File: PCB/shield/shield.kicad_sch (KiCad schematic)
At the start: 19 parts, among them J1 QTR-8A, J10 ESP32_left_m, J11 ESP32_right_m, J13 Conn_01x06, J14 Domino, J15 Domino, J2 QMC5883L, J3 Servo, J4 Domino, J8 ESP32_left_f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

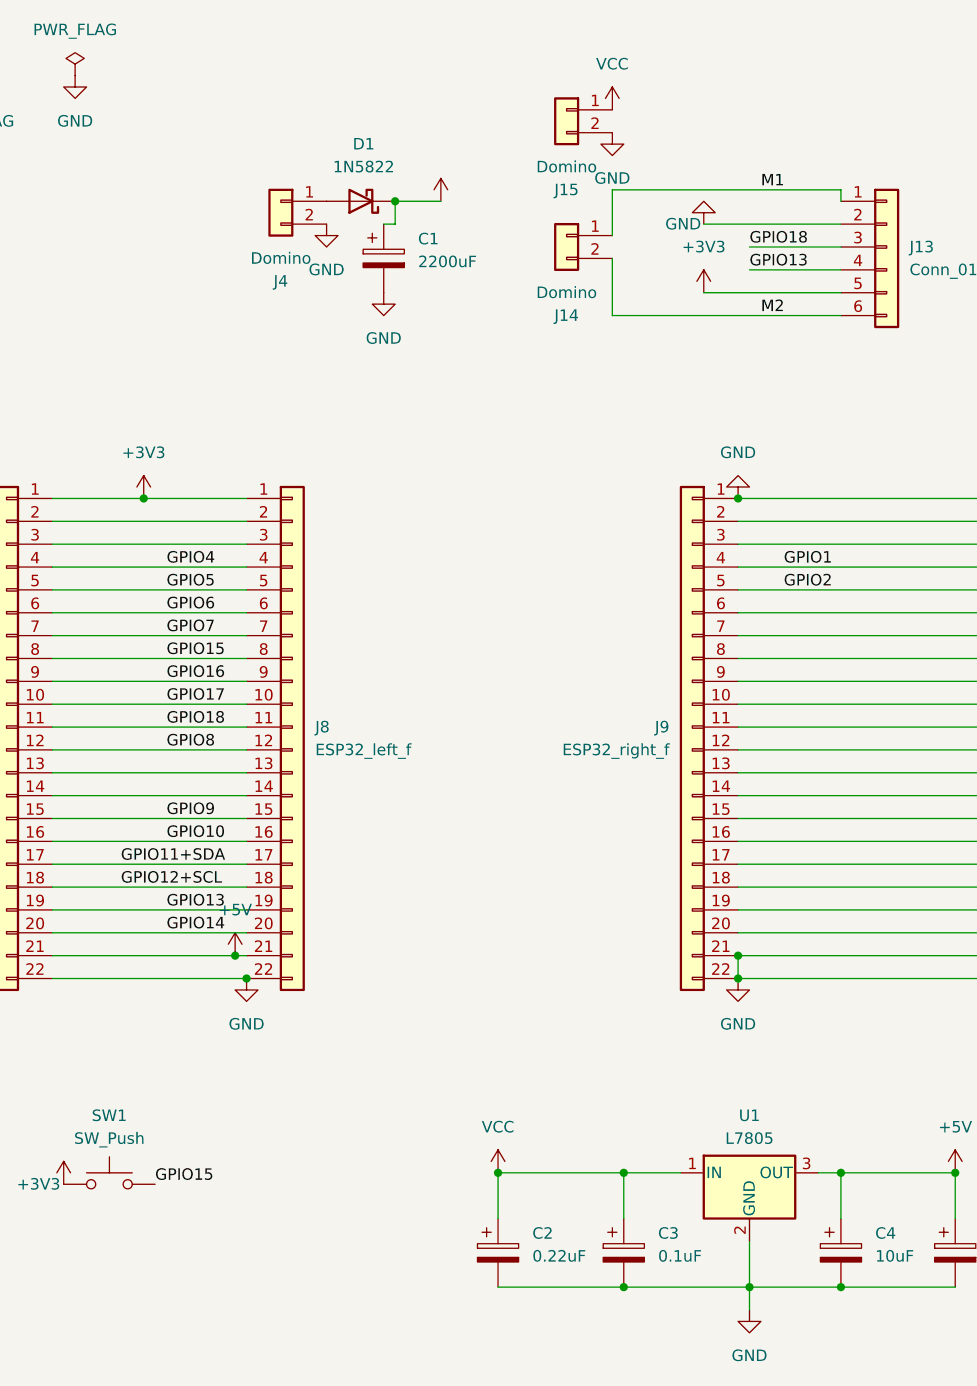
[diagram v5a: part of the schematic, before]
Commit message: feat: change THT to SMD
Changed LM7805 to AMS1117
Changed THT capacitor to SMD capacitor
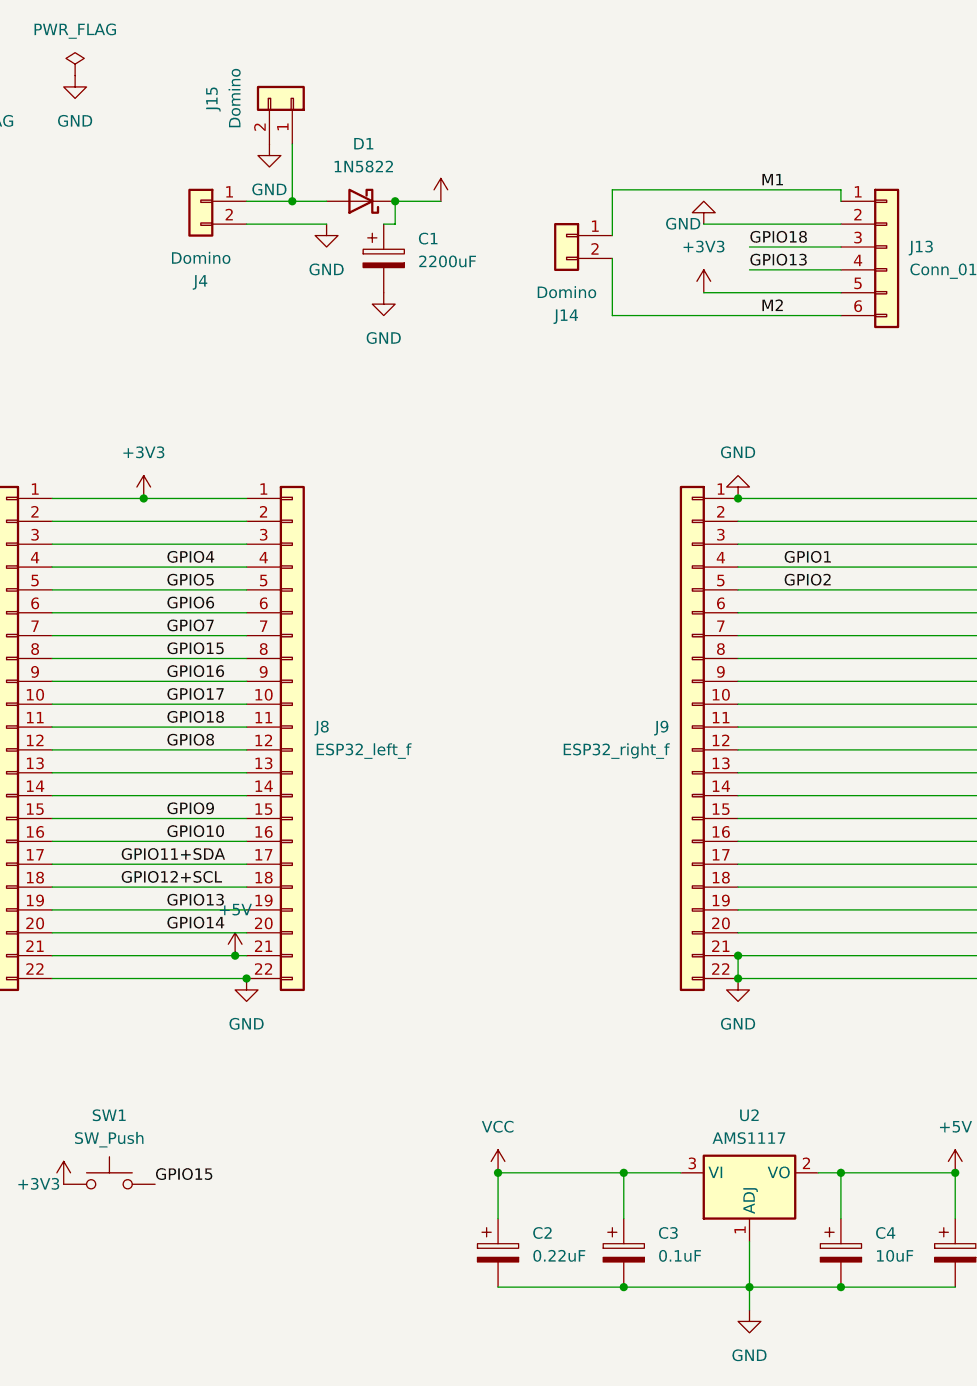
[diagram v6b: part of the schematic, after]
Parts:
- removed U1: L7805, Package_TO_SOT_THT:TO-220-3_Vertical, symbol Regulator_Linear:L7805
- added U2: AMS1117, Package_TO_SOT_SMD:SOT-223-3_TabPin2, symbol Regulator_Linear:AMS1117
- C2, C4: footprint Capacitor_THT:CP_Radial_D5.0mm_P2.00mm -> Capacitor_SMD:C_0805_2012Metric_Pad1.18x1.45mm_HandSolder
- C3, C5: footprint Capacitor_THT:CP_Radial_Tantal_D4.5mm_P2.50mm -> Capacitor_SMD:C_0805_2012Metric_Pad1.18x1.45mm_HandSolder
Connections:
- net +5V: now also U2.2 (VO)
- net GND: now also U2.1 (ADJ)
- net VCC: now also U2.3 (VI); no longer J15.1 (Pin_1)
- net at D1.2 (A), J4.1 (Pin_1): now also J15.1 (Pin_1)
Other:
- moved on the sheet: J15, J4
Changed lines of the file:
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@@
 	)
 	(junction
+		(at 87.63 39.37)
+		(diameter 0)
+		(color 0 0 0 0)
+	)
+	(junction
 		(at 138.43 160.02)
 		(diameter 0)
@@
 	(wire
 		(pts
+			(xy 82.55 41.91) (xy 91.44 41.91)
+		)
+		(stroke
+			(width 0)
+			(type default)
+		)
+	)
+	(wire
+		(pts
 			(xy 60.96 123.19) (xy 81.28 123.19)
 		)
@@
 	(wire
 		(pts
+			(xy 82.55 39.37) (xy 87.63 39.37)
+		)
+		(stroke
+			(width 0)
+			(type default)
+		)
+	)
+	(wire
+		(pts
 			(xy 138.43 46.99) (xy 148.59 46.99)
 		)
@@
 	(wire
 		(pts
+			(xy 87.63 39.37) (xy 91.44 39.37)
+		)
+		(stroke
+			(width 0)
+			(type default)
+		)
+	)
+	(wire
+		(pts
 			(xy 166.37 80.01) (xy 137.16 80.01)
 		)
@@
 	(wire
 		(pts
+			(xy 87.63 33.02) (xy 87.63 39.37)
+		)
+		(stroke
+			(width 0)
+			(type default)
+		)
+	)
+	(wire
+		(pts
 			(xy 60.96 82.55) (xy 82.55 82.55)
 		)
@@
 			)
 		)
-		(property "Footprint" "Capacitor_THT:CP_Radial_Tantal_D4.5mm_P2.50mm"
+		(property "Footprint" "Capacitor_SMD:C_0805_2012Metric_Pad1.18x1.45mm_HandSolder"
 			(at 162.2552 160.02 0)
 			(effects
@@
 	)
 	(symbol
-		(lib_id "power:VCC")
-		(at 123.19 29.21 0)
-		(unit 1)
-		(exclude_from_sim no)
-		(in_bom yes)
-		(on_board yes)
-		(dnp no)
-		(fields_autoplaced yes)
-		(property "Reference" "#PWR022"
-			(at 123.19 33.02 0)
-			(effects
-				(font
-					(size 1.27 1.27)
-				)
-				(hide yes)
-			)
-		)
-		(property "Value" "VCC"
-			(at 123.19 24.13 0)
-			(effects
-				(font
-					(size 1.27 1.27)
-				)
-			)
-		)
-		(property "Footprint" ""
-			(at 123.19 29.21 0)
-			(effects
-				(font
-					(size 1.27 1.27)
-				)
-				(hide yes)
-			)
-		)
-		(property "Datasheet" ""
-			(at 123.19 29.21 0)
-			(effects
-				(font
-					(size 1.27 1.27)
-				)
-				(hide yes)
-			)
-		)
-		(property "Description" "Power symbol creates a global label with name \"VCC\""
-			(at 123.19 29.21 0)
-			(effects
-				(font
-					(size 1.27 1.27)
-				)
-				(hide yes)
-			)
-		)
-		(pin "1"
-		)
-		(instances
-			(project ""
-				(path "/9a41b561-8e6b-4187-bd8f-1a6b5b887c54"
-					(reference "#PWR022")
-					(unit 1)
-				)
-			)
-		)
-	)
-	(symbol
 		(lib_id "Connector_Generic:Conn_01x03")
 		(at 228.6 120.65 0)
@@
 	(symbol
 		(lib_id "Connector_Generic:Conn_01x02")
-		(at 118.11 29.21 0)
-		(mirror y)
+		(at 87.63 27.94 270)
+		(mirror x)
 		(unit 1)
 		(exclude_from_sim no)
@@
 		(dnp no)
 		(property "Reference" "J15"
-			(at 118.11 38.1 0)
+			(at 78.74 27.94 0)
 			(effects
 				(font
@@
 		)
 		(property "Value" "Domino"
-			(at 118.11 35.56 0)
+			(at 81.28 27.94 0)
 			(effects
 				(font
@@
 		)
 		(property "Footprint" "TerminalBlock_Phoenix:TerminalBlock_Phoenix_MKDS-1,5-2_1x02_P5.00mm_Horizontal"
-			(at 118.11 29.21 0)
+			(at 87.63 27.94 0)
 			(effects
 				(font
@@
 		)
 		(property "Datasheet" "~"
-			(at 118.11 29.21 0)
+			(at 87.63 27.94 0)
 			(effects
 				(font
@@
 		)
 		(property "Description" "Generic connector, single row, 01x02, script generated (kicad-library-utils/schlib/autogen/connector/)"
-			(at 118.11 29.21 0)
+			(at 87.63 27.94 0)
 			(effects
 				(font
@@
 	(symbol
 		(lib_id "Connector_Generic:Conn_01x02")
-		(at 86.36 39.37 0)
+		(at 77.47 39.37 0)
 		(mirror y)
 		(unit 1)
@@
 		(dnp no)
 		(property "Reference" "J4"
-			(at 86.36 48.26 0)
+			(at 77.47 48.26 0)
 			(effects
 				(font
@@
 		)
 		(property "Value" "Domino"
-			(at 86.36 45.72 0)
+			(at 77.47 45.72 0)
 			(effects
 				(font
@@
 		)
 		(property "Footprint" "TerminalBlock_Phoenix:TerminalBlock_Phoenix_MKDS-1,5-2_1x02_P5.00mm_Horizontal"
-			(at 86.36 39.37 0)
+			(at 77.47 39.37 0)
 			(effects
 				(font
@@
 		)
 		(property "Datasheet" "~"
-			(at 86.36 39.37 0)
+			(at 77.47 39.37 0)
 			(effects
 				(font
@@
 		)
 		(property "Description" "Generic connector, single row, 01x02, script generated (kicad-library-utils/schlib/autogen/connector/)"
-			(at 86.36 39.37 0)
+			(at 77.47 39.37 0)
 			(effects
 				(font
@@
 			)
 		)
-		(property "Footprint" "Capacitor_THT:CP_Radial_Tantal_D4.5mm_P2.50mm"
+		(property "Footprint" "Capacitor_SMD:C_0805_2012Metric_Pad1.18x1.45mm_HandSolder"
 			(at 125.4252 160.02 0)
 			(effects
@@
 			)
 		)
-		(property "Footprint" "Capacitor_THT:CP_Radial_D5.0mm_P2.00mm"
+		(property "Footprint" "Capacitor_SMD:C_0805_2012Metric_Pad1.18x1.45mm_HandSolder"
 			(at 149.5552 160.02 0)
 			(effects
@@
 	)
 	(symbol
-		(lib_id "Regulator_Linear:L7805")
-		(at 138.43 147.32 0)
-		(unit 1)
-		(exclude_from_sim no)
-		(in_bom yes)
-		(on_board yes)
-		(dnp no)
-		(fields_autoplaced yes)
-		(property "Reference" "U1"
-			(at 138.43 140.97 0)
-			(effects
-				(font
-					(size 1.27 1.27)
-				)
-			)
-		)
-		(property "Value" "L7805"
-			(at 138.43 143.51 0)
-			(effects
-				(font
-					(size 1.27 1.27)
-				)
-			)
-		)
-		(property "Footprint" "Package_TO_SOT_THT:TO-220-3_Vertical"
-			(at 139.065 151.13 0)
-			(effects
-				(font
-					(size 1.27 1.27)
-					(italic yes)
-				)
-				(justify left)
-				(hide yes)
-			)
-		)
-		(property "Datasheet" "http://www.st.com/content/ccc/resource/technical/document/datasheet/41/4f/b3/b0/12/d4/47/88/CD00000444.pdf/files/CD00000444.pdf/jcr:content/translations/en.CD00000444.pdf"
-			(at 138.43 148.59 0)
-			(effects
-				(font
-					(size 1.27 1.27)
-				)
-				(hide yes)
-			)
-		)
-		(property "Description" "Positive 1.5A 35V Linear Regulator, Fixed Output 5V, TO-220/TO-263/TO-252"
-			(at 138.43 147.32 0)
-			(effects
-				(font
-					(size 1.27 1.27)
-				)
-				(hide yes)
-			)
-		)
-		(pin "2"
-		)
-		(pin "1"
-		)
-		(pin "3"
-		)
-		(instances
-			(project ""
-				(path "/9a41b561-8e6b-4187-bd8f-1a6b5b887c54"
-					(reference "U1")
-					(unit 1)
-				)
-			)
-		)
-	)
-	(symbol
 		(lib_id "Connector_Generic:Conn_01x05")
 		(at 207.01 86.36 0)
@@
 	(symbol
 		(lib_id "power:GND")
-		(at 123.19 31.75 0)
+		(at 85.09 33.02 0)
 		(unit 1)
 		(exclude_from_sim no)
@@
 		(on_board yes)
 		(dnp no)
-		(fields_autoplaced yes)
 		(property "Reference" "#PWR023"
-			(at 123.19 38.1 0)
+			(at 85.09 39.37 0)
 			(effects
 				(font
@@
 		)
 		(property "Value" "GND"
-			(at 123.19 36.83 0)
+			(at 85.09 38.1 0)
 			(effects
 				(font
@@
 		)
 		(property "Footprint" ""
-			(at 123.19 31.75 0)
+			(at 85.09 33.02 0)
 			(effects
 				(font
@@
 		)
 		(property "Datasheet" ""
-			(at 123.19 31.75 0)
+			(at 85.09 33.02 0)
 			(effects
 				(font
@@
 		)
 		(property "Description" "Power symbol creates a global label with name \"GND\" , ground"
-			(at 123.19 31.75 0)
+			(at 85.09 33.02 0)
 			(effects
 				(font
@@
 			)
 		)
-		(property "Footprint" "Capacitor_THT:CP_Radial_D5.0mm_P2.00mm"
+		(property "Footprint" "Capacitor_SMD:C_0805_2012Metric_Pad1.18x1.45mm_HandSolder"
 			(at 111.4552 160.02 0)
 			(effects
@@
 					(unit 1)
 				)
+			)
+		)
+	)
+	(symbol
+		(lib_id "Regulator_Linear:AMS1117")
+		(at 138.43 147.32 0)
+		(unit 1)
+		(exclude_from_sim no)
+		(in_bom yes)
+		(on_board yes)
+		(dnp no)
+		(fields_autoplaced yes)
+		(property "Reference" "U2"
+			(at 138.43 140.97 0)
+			(effects
+				(font
+					(size 1.27 1.27)
+				)
+			)
+		)
+		(property "Value" "AMS1117"
+			(at 138.43 143.51 0)
+			(effects
+				(font
+					(size 1.27 1.27)
+				)
+			)
+		)
+		(property "Footprint" "Package_TO_SOT_SMD:SOT-223-3_TabPin2"
+			(at 138.43 142.24 0)
+			(effects
+				(font
+					(size 1.27 1.27)
+				)
+				(hide yes)
+			)
+		)
+		(property "Datasheet" "http://www.advanced-monolithic.com/pdf/ds1117.pdf"
+			(at 140.97 153.67 0)
+			(effects
+				(font
+					(size 1.27 1.27)
+				)
+				(hide yes)
+			)
+		)
+		(property "Description" "1A Low Dropout regulator, positive, adjustable output, SOT-223"
+			(at 138.43 147.32 0)
+			(effects
+				(font
+					(size 1.27 1.27)
+				)
+				(hide yes)
+			)
+		)
+		(pin "3"
+		)
+		(pin "2"
+		)
+		(pin "1"
+		)
+		(instances
+			(project ""
+				(path "/9a41b561-8e6b-4187-bd8f-1a6b5b887c54"
+					(reference "U2")
+					(unit 1)
+				)

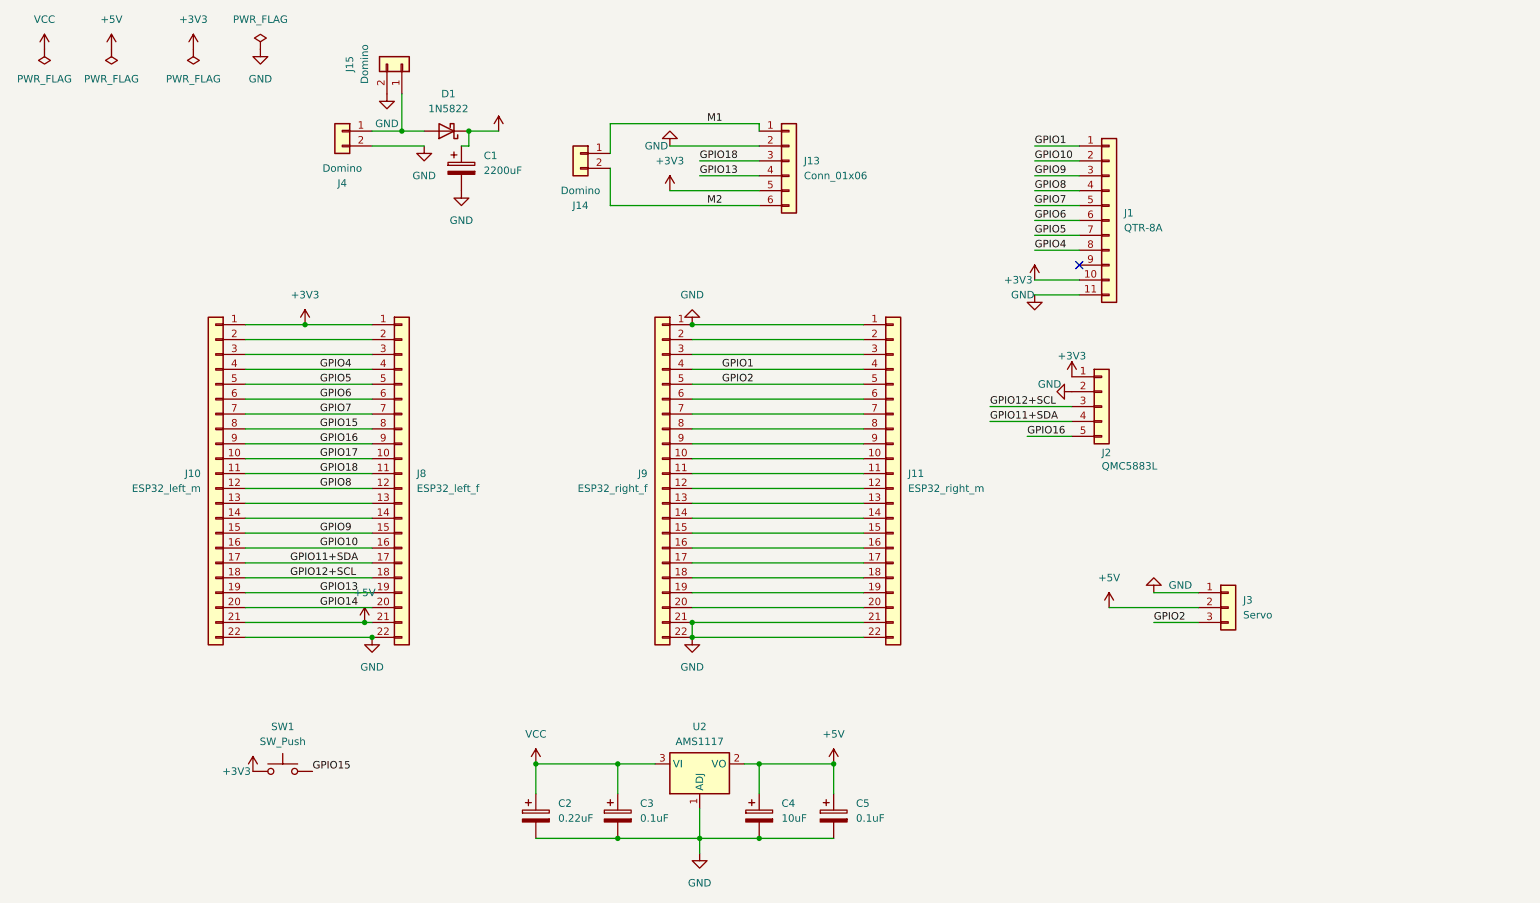
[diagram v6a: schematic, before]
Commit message: feat: added socket for joystick module
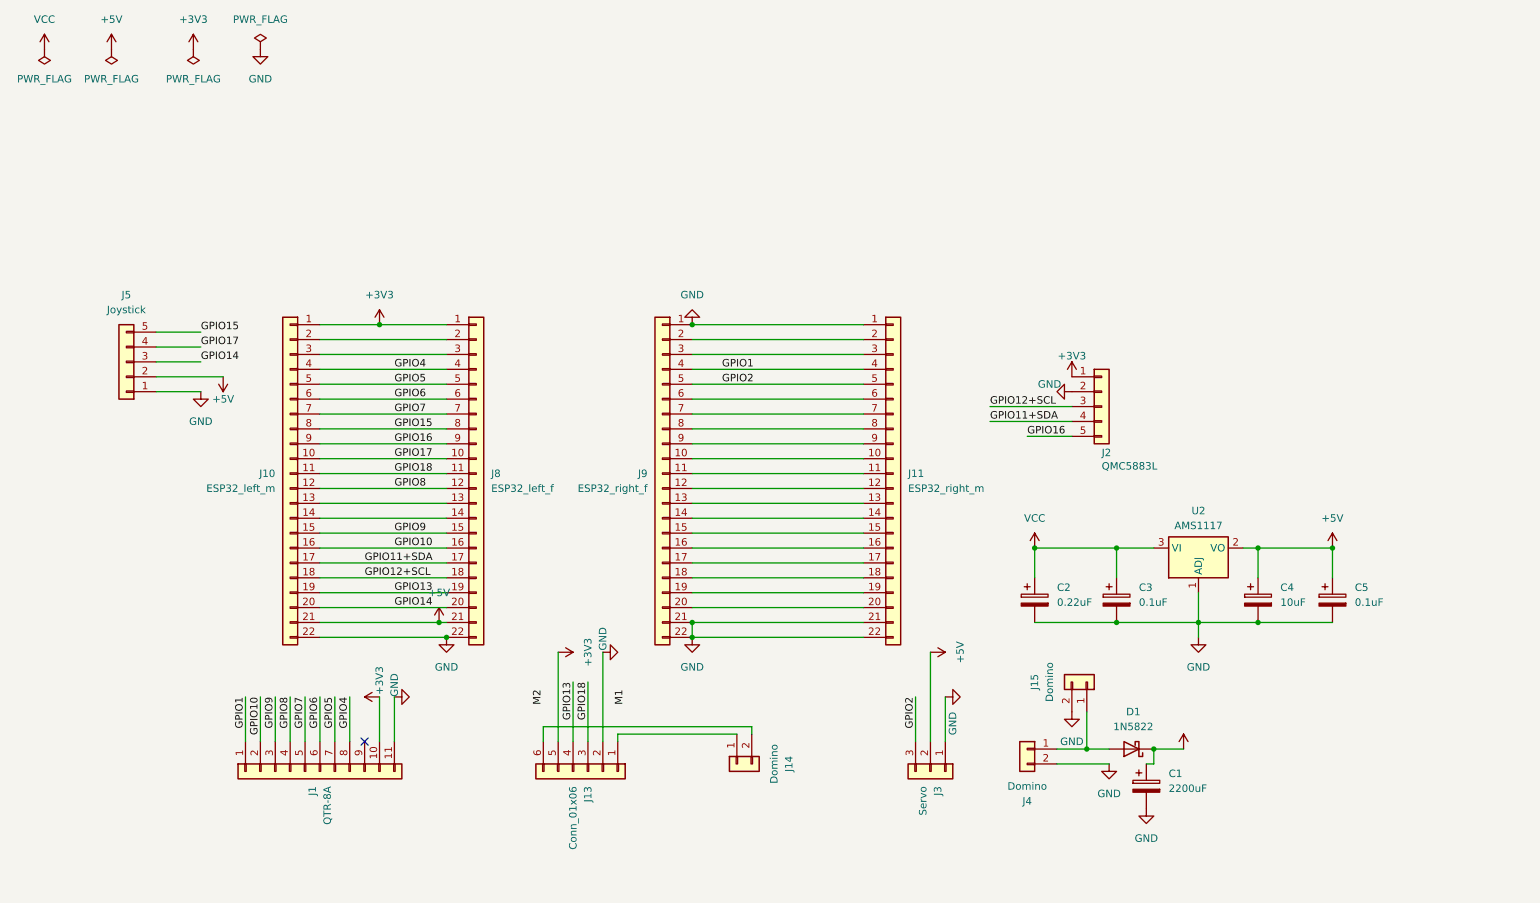
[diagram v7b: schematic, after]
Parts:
- removed SW1: SW_Push, Button_Switch_THT:SW_PUSH_6mm_H5mm, symbol Switch:SW_Push
- added J5: Joystick, Connector_PinSocket_2.54mm:PinSocket_1x05_P2.54mm_Vertical, symbol Connector_Generic:Conn_01x05
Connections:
- net +5V: now also J5.2 (Pin_2)
- net GND: now also J5.1 (Pin_1)
- net GPIO14: now also J5.3 (Pin_3)
- net GPIO15: now also J5.5 (Pin_5)
- net GPIO17: now also J5.4 (Pin_4)
- net M1: no longer J13.1 (Pin_1), J14.1 (Pin_1)
- net M2: no longer J13.6 (Pin_6), J14.2 (Pin_2)
- new net: J13.1 (Pin_1), J14.1 (Pin_1)
- new net: J13.6 (Pin_6), J14.2 (Pin_2)
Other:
- moved on the sheet: C1, C2, C3, C4, C5, D1, J1, J10, J13, J14, J15, J3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

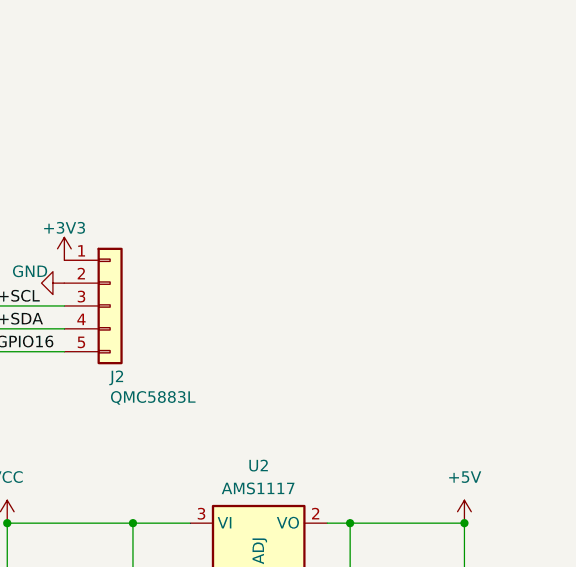
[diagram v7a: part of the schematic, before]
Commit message: feat: add lcd oled screen socket
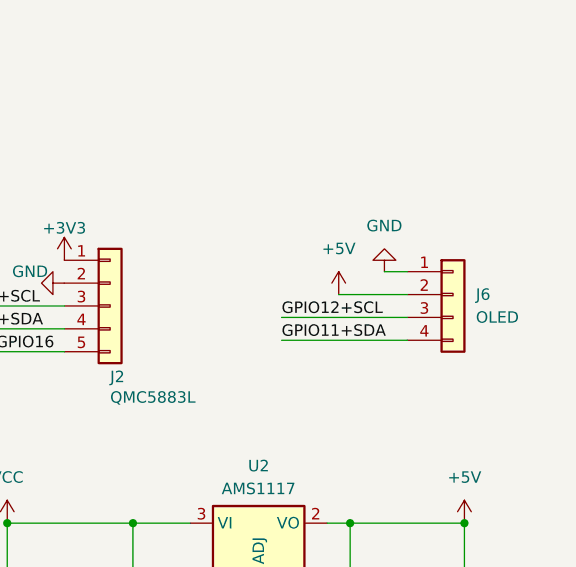
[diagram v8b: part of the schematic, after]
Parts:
- added J6: OLED, Connector_PinSocket_2.54mm:PinSocket_1x04_P2.54mm_Vertical, symbol Connector_Generic:Conn_01x04
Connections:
- net +5V: now also J6.2 (Pin_2)
- net GND: now also J6.1 (Pin_1)
- net GPIO11+SDA: now also J6.4 (Pin_4)
- net GPIO12+SCL: now also J6.3 (Pin_3)
